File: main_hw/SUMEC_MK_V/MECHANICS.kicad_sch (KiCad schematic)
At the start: 20 parts, among them SW2 SW_Push, SW3 SW_Push, SW4 SW_Push, SW5 SW_Push

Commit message: new qre board
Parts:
- added TP18: TestPoint, TestPoint:TestPoint_Pad_D1.0mm, symbol Connector:TestPoint
- TP10, TP11, TP12, TP13, TP14, TP15, TP16, TP17, TP7, TP8, TP9: footprint TestPoint:TestPoint_Pad_1.0x1.0mm -> TestPoint:TestPoint_Pad_D1.0mm
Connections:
- net MOTOR_L_2: now also TP16.1
- net MOTOR_R_1: no longer TP9.1
- net MOTOR_R_2: now also TP18.1
- net BTN_IOXX renamed BTN_IO04
- net BTN_IOXY renamed BTN_IO05
- new net +12V: TP9.1
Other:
- moved on the sheet: H1, H2, TP10, TP11, TP12, TP13, TP14, TP15, TP16, TP17, TP7, TP8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

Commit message: 67yfhtgftu
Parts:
- added TP24: TestPoint, TestPoint:TestPoint_Pad_D1.0mm, symbol Connector:TestPoint
- renumbered R27 to R28, TP7 to TP11, TP8 to TP13, TP13 to TP14, TP9 to TP15, TP14 to TP16, TP11 to TP17, TP15 to TP18, TP10 to TP19, TP16 to TP20, TP17 to TP21, TP18 to TP22
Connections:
- net EN_L: now also TP12.1; no longer TP16.1
- net EN_R: now also TP16.1; no longer TP12.1
- net MOTOR_L_1: now also TP21.1; no longer TP19.1
- net MOTOR_L_2: now also TP22.1; no longer TP20.1
- net MOTOR_R_1: now also TP19.1; no longer TP21.1
- net MOTOR_R_2: now also TP20.1; no longer TP22.1
- net PH_L: now also TP14.1; no longer TP18.1
- net PH_R: now also TP18.1; no longer TP14.1
- new net VBUS_USB: TP24.1
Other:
- moved on the sheet: C26, C27, H1, H2, R28, SW2, SW3, SW4, SW5, TP11, TP12, TP13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

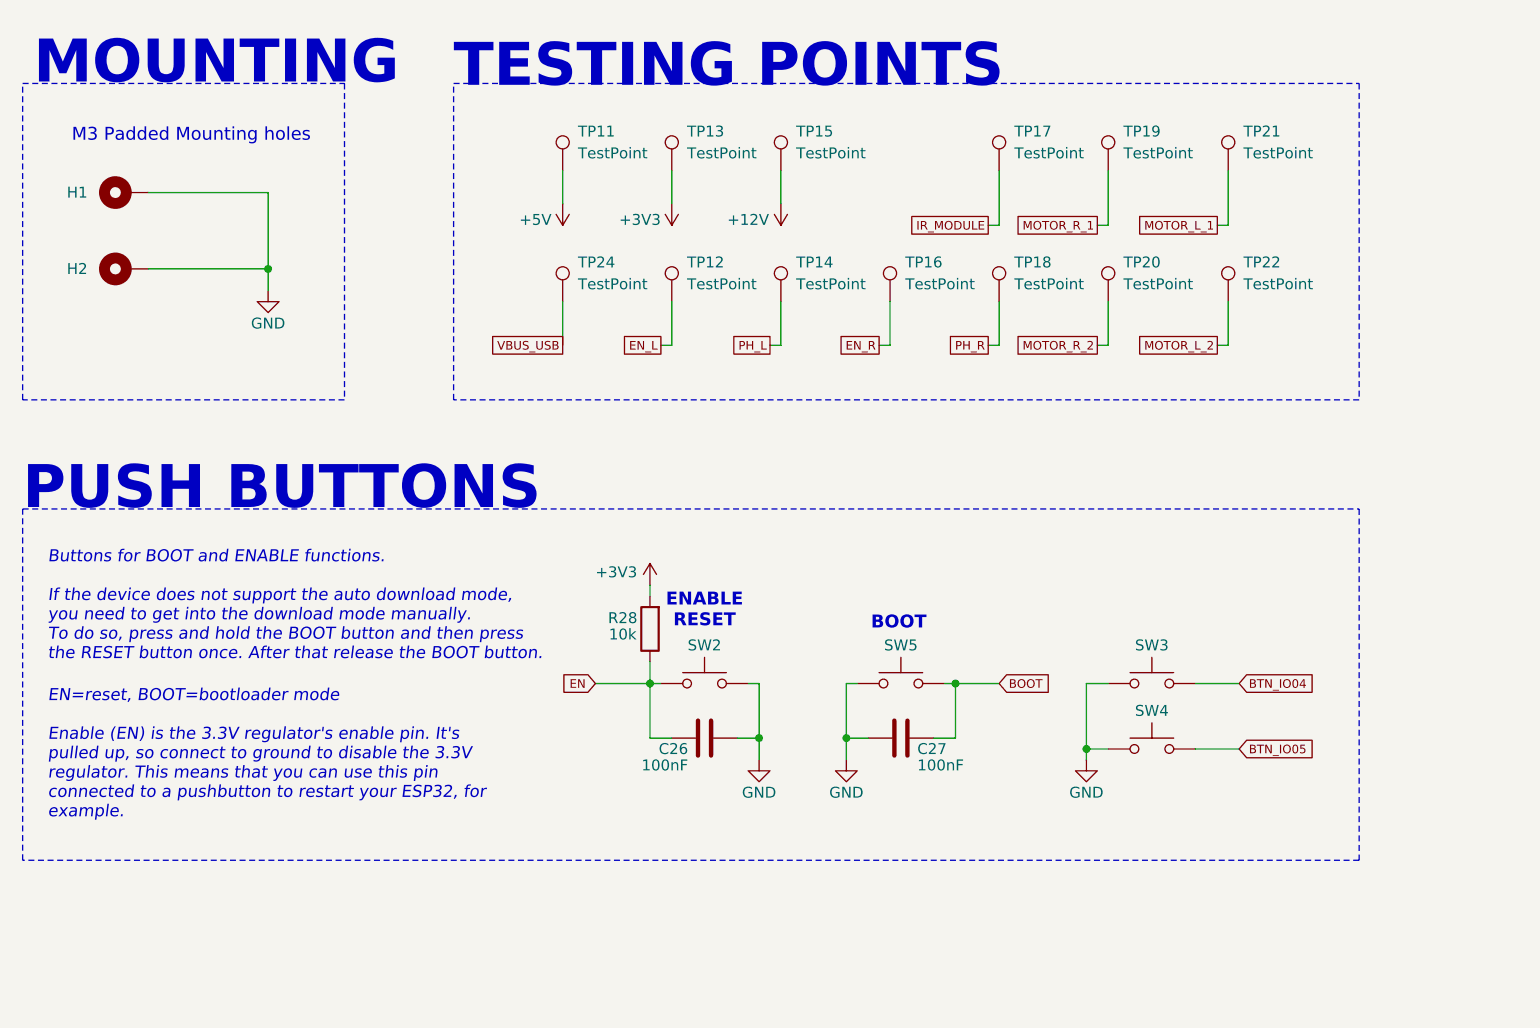
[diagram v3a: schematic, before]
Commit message: MK5 bugfix fixed POL_L, minor changes, deleted nSLEEP and nFault connections to the MCU
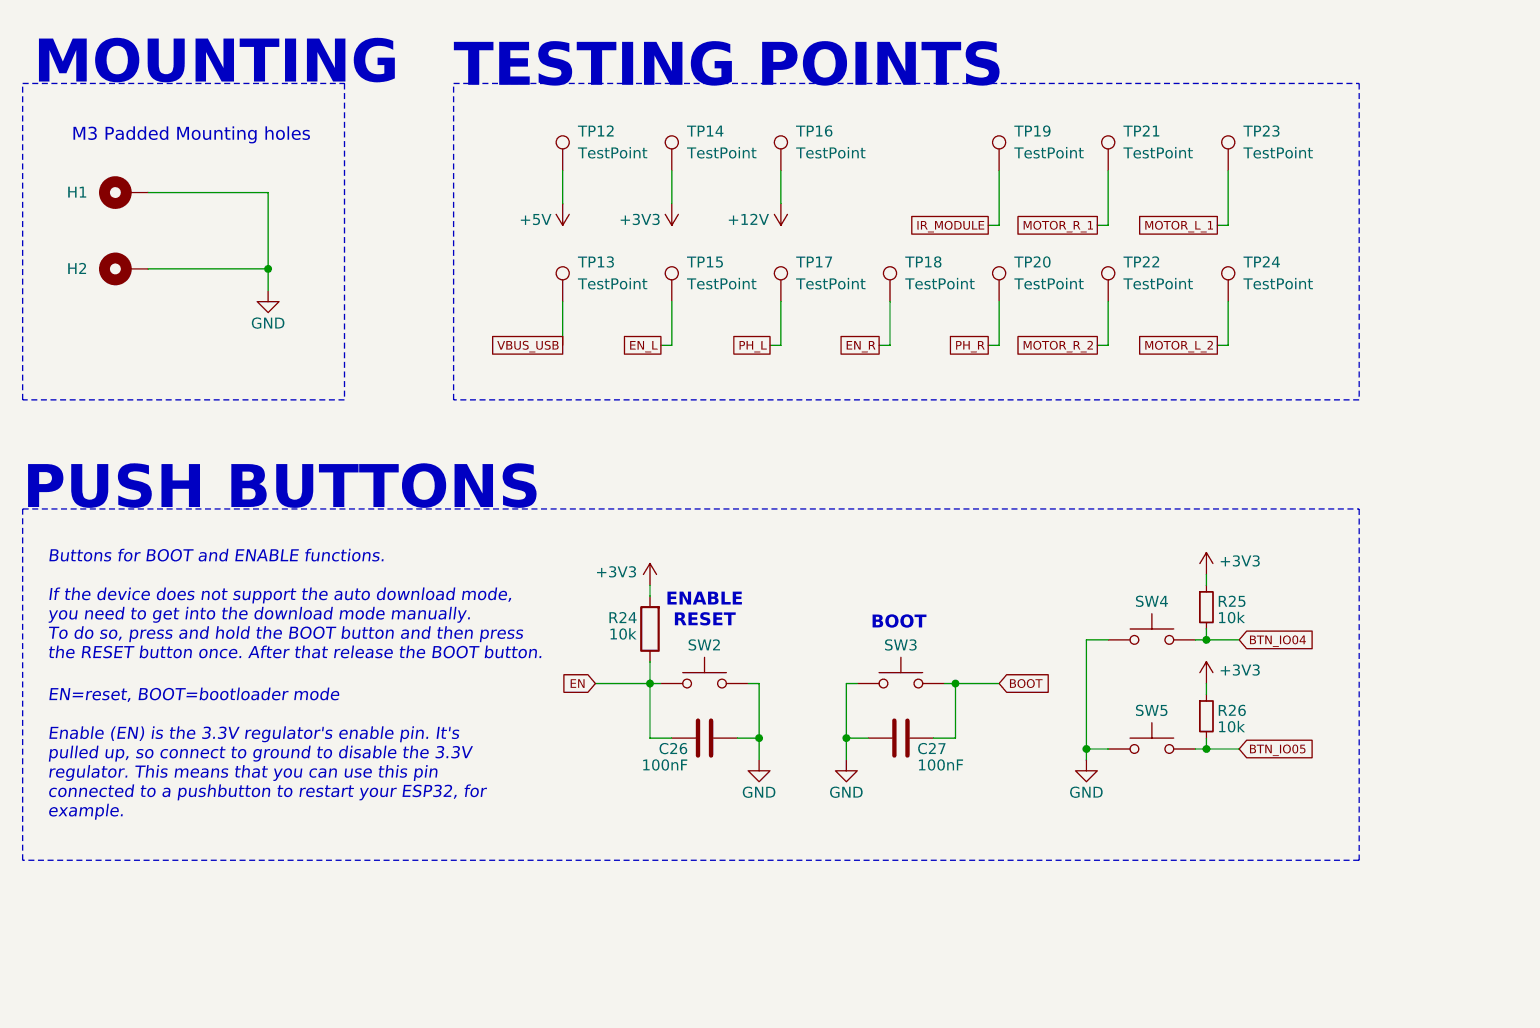
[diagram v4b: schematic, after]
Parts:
- added R25, R26: 10k, Resistor_SMD:R_0805_2012Metric_Pad1.20x1.40mm_HandSolder, symbol Device:R_Small
- renumbered R28 to R24, SW5 to SW3, SW3 to SW4, SW4 to SW5, TP11 to TP12, TP24 to TP13, TP13 to TP14, TP12 to TP15, TP15 to TP16, TP14 to TP17, TP16 to TP18, TP17 to TP19, TP18 to TP20, TP19 to TP21, TP20 to TP22, TP21 to TP23, TP22 to TP24
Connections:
- net +3V3: now also R25.1, R26.1
- net BTN_IO04: now also R25.2
- net BTN_IO05: now also R26.2
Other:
- moved on the sheet: SW4

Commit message: updates to mk5
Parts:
- added R24: 10k, Resistor_SMD:R_0805_2012Metric_Pad1.20x1.40mm_HandSolder, symbol Device:R
- renumbered C26 to C25, C27 to C26, R24 to R23
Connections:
- net +3V3: now also R24.2
- net BOOT: now also R24.1
